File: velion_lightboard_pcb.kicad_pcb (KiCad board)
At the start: 2 copper layers, 100 x 100 mm, 137 parts, among them J1 Conn_01x04, J10 Conn_01x04, J11 Conn_01x04, J12 Conn_01x03, J13 Conn_01x03, J14 Conn_01x03, J15 Conn_01x03, J16 Conn_01x03, J17 Conn_01x04, J2 Conn_01x04, J3 Conn_01x03, J4 Conn_01x04, J5 Conn_01x04, J6 Conn_01x04, J7 Conn_01x03, J8 Conn_01x03, J9 Conn_01x03, Q1 BSS123-7-F, Q10 BSS123-7-F, Q11 BSS123-7-F, Q12 BSS123-7-F, Q13 NMOS, Q14 NMOS, Q15 NMOS, Q16 NMOS, Q17 NMOS, Q18 NMOS, Q19 NMOS, Q2 BSS123-7-F, Q20 NMOS, Q3 BSS123-7-F, Q4 BSS123-7-F, Q5 BSS123-7-F, Q6 BSS123-7-F, Q7 BSS123-7-F, Q8 BSS123-7-F, Q9 BSS123-7-F, U1 ESP32-C3_SUPERMINI_TH, U10 LM2104DR, U11 ADS1115IDGS, U12 MCP23017_SO, U13 ADS1115IDGS, U14 TJA1051T-3, U2 MCP6L01x-xOT, U3 MCP6L01x-xOT, U4 MCP6L01x-xOT, U5 LM2104DR, U6 LM2104DR, U7 LM2104DR, U8 LM2104DR, U9 LM2104DR

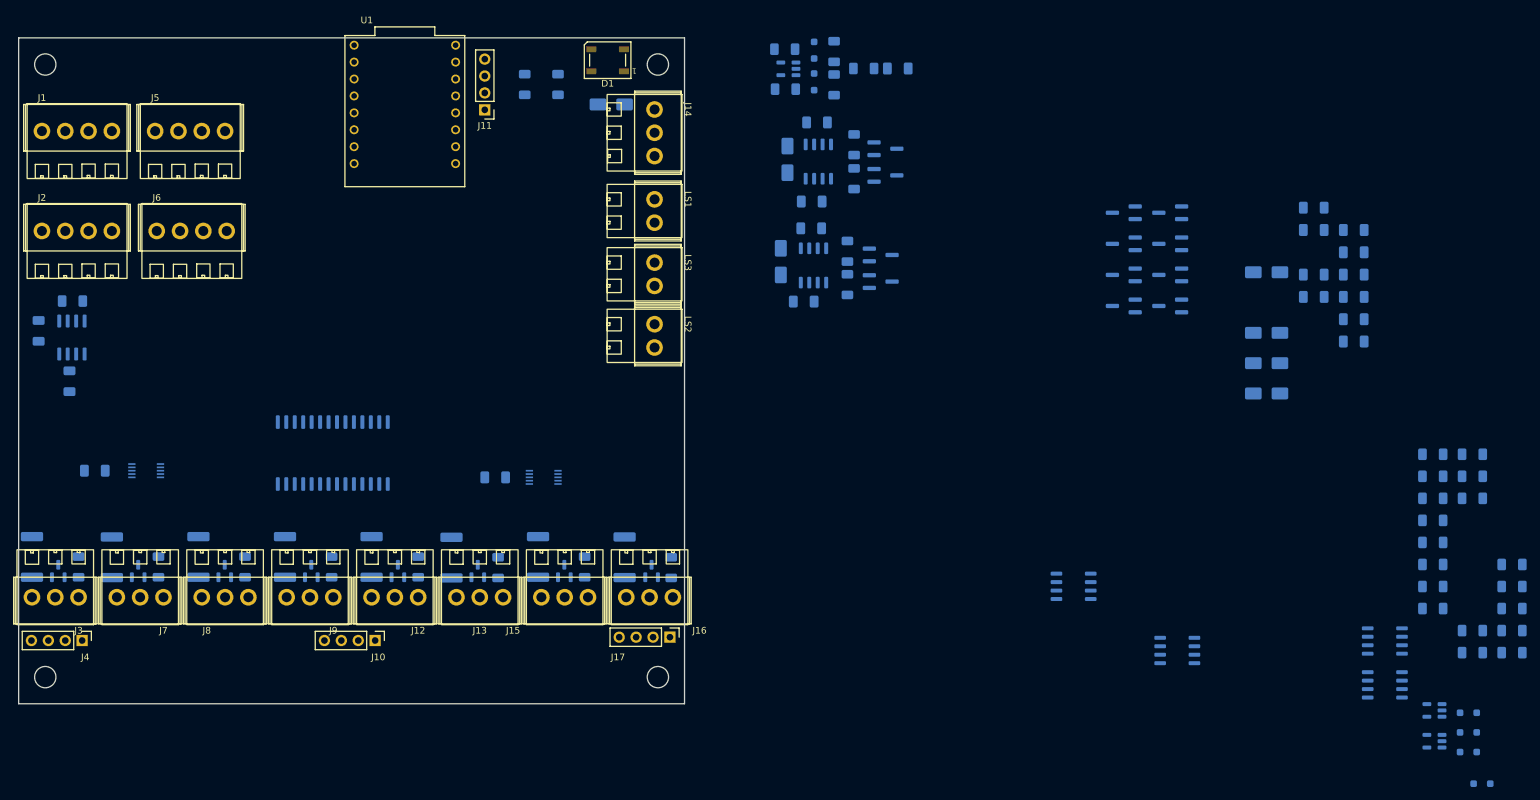
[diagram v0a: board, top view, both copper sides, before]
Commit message: routed the PCB, need review
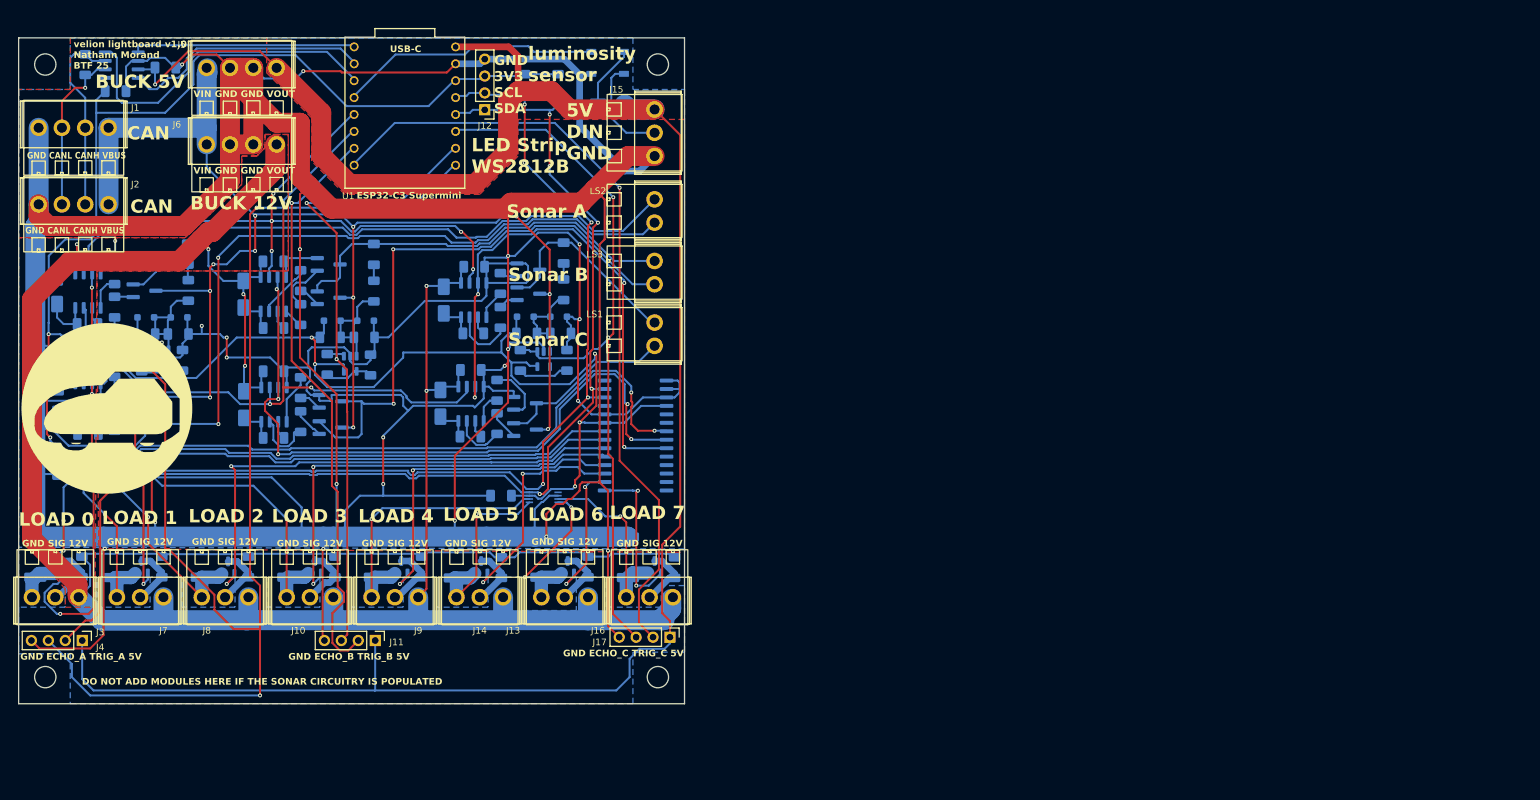
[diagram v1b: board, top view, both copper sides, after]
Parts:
- added G***: LOGO, velion_mainboard:silhouette, F.Cu at (63.2, 111.0)
- D1: moved to B.Cu
- moved R18 186.9 mm to (92.3, 86.5), turned to -90 degrees
- moved R21 186.5 mm to (92.3, 91.5), turned to 90 degrees
- moved R20 184.9 mm to (92.3, 102.5), turned to -90 degrees
- moved R19 184.6 mm to (92.3, 107.6), turned to 90 degrees
- moved D7 180.5 mm to (97.1, 92.5), turned to 0 degrees
- moved R24 177.9 mm to (96.8, 95.0)
- moved D6 176.8 mm to (102.1, 92.5)
- moved R17 172.7 mm to (103.3, 88.0), turned to 90 degrees
- moved U7 170.9 mm to (99.8, 98.9), turned to -90 degrees
- moved U11 170.6 mm to (88.3, 105.1), turned to -90 degrees
- moved R22 166.9 mm to (96.3, 99.0), turned to 90 degrees
- moved C11 164.1 mm to (88.3, 110.1), turned to 0 degrees
- moved C12 162.6 mm to (88.3, 93.6), turned to 0 degrees
- moved C13 162.6 mm to (88.3, 100.1), turned to 0 degrees
- moved C10 162.3 mm to (88.2, 83.6), turned to 0 degrees
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- renumbered C19 to C0, C7 to C1, C1 to C10, C9 to C11, C3 to C12, C8 to C13, C10 to C14, C4 to C15, C11 to C16, C14 to C17, C12 to C18, C16 to C2, C13 to C3, C17 to C4, C18 to C6, C6 to C7, C2 to C8, C15 to C9, D12 to D0, D3 to D10, D9 to D12, D8 to D13, D7 to D2, D6 to D3, D14 to D4, D13 to D5, D5 to D6, D4 to D7, D10 to D8, D2 to D9, J9 to J10, J10 to J11, J11 to J12, J15 to J13, J13 to J14, J14 to J15, J12 to J9, LS3 to LS1, LS1 to LS2, LS2 to LS3, Q13 to Q0, Q10 to Q1, Q7 to Q10, Q16 to Q11, Q17 to Q12, Q2 to Q13, Q1 to Q14, Q8 to Q15, Q5 to Q16, Q18 to Q17, Q19 to Q18, Q20 to Q19, Q9 to Q2, Q12 to Q3, Q11 to Q4, Q14 to Q5, Q15 to Q6, Q3 to Q7, Q4 to Q8, Q6 to Q9, R29 to R0, R30 to R1, R12 to R10, R22 to R11, R25 to R12, R36 to R13, R34 to R14, R35 to R15, R31 to R16, R26 to R17, R6 to R18, R9 to R19, R32 to R2, R10 to R20, R5 to R21, R14 to R22, R13 to R23, R27 to R24, R15 to R25, R38 to R26, R40 to R27, R39 to R28, R37 to R29, R33 to R3, R20 to R30, R19 to R31, R24 to R32, R18 to R33, R28 to R34, R43 to R35, R42 to R36, R41 to R37, R44 to R38, R2 to R39, R11 to R4, R4 to R40, R1 to R41, R7 to R42, R3 to R43, R45 to R44, R46 to R45, R23 to R5, R17 to R6, R8 to R7, R21 to R8, R16 to R9, U3 to U10, U8 to U11, U5 to U12, U6 to U13, U13 to U14, U12 to U2, U10 to U3, U9 to U4, U4 to U5, U11 to U6, U2 to U7, U14 to U8, U7 to U9
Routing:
- net GND: track 0.00 -> 1058.9 mm, vias 0 -> 27
- net +12V: track 0.00 -> 536.6 mm, vias 0 -> 7
- net +3.3V: track 0.00 -> 331.2 mm, vias 0 -> 9
- net +5V: track 0.00 -> 315.8 mm, vias 0 -> 1
- net VBUS: track 0.00 -> 212.6 mm, vias 0 -> 11
- net ECHO_A: track 0.00 -> 199.2 mm, vias 0 -> 3
- net PIEZO_PWM_HALF_Y: track 0.00 -> 158.8 mm, vias 0 -> 4
- net SDA: track 0.00 -> 154.0 mm, vias 0 -> 5
- net SCL: track 0.00 -> 150.2 mm, vias 0 -> 5
- net EN_PIEZO_A: track 0.00 -> 129.0 mm, vias 0 -> 5
- net TRIG_C: track 0.00 -> 118.7 mm, vias 0 -> 1
- net MOSFET_GATE_0: track 0.00 -> 114.3 mm, vias 0 -> 2
- net Net-(LS1-Pad2): track 0.00 -> 112.2 mm, vias 0 -> 2
- net ECHO_C: track 0.00 -> 111.5 mm, vias 0 -> 2
- net EN_PIEZO_B: track 0.00 -> 104.9 mm, vias 0 -> 5
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- added copper zone on B.Cu, net +12V
- added copper zone on F.Cu, net +12V
- added copper zone on B.Cu, net GND
- added copper zone on F.Cu, net GND
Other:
- board text added: "5V DIN GND"
- board text added: "BUCK 12V"
- board text added: "BUCK 5V"
- board text added: "CAN"
- board text added: "DO NOT ADD MODULES HERE IF THE SONAR CIRCUITRY IS POPULATED"
- board text added: "ESP32-C3 Supermini"
- board text added: "GND 3V3 SCL SDA"
- board text added: "GND CANL CANH VBUS"
- board text added: "GND ECHO_A TRIG_A 5V"
- board text added: "GND ECHO_B TRIG_B 5V"
- board text added: "GND ECHO_C TRIG_C 5V"
- board text added: "GND SIG 12V"
- board text added: "LED Strip WS2812B"
- board text added: "LOAD 0"
- board text added: "LOAD 1"
- board text added: "LOAD 2"
- board text added: "LOAD 3"
- board text added: "LOAD 4"
- board text added: "LOAD 5"
- board text added: "LOAD 6"
- board text added: "LOAD 7"
- board text added: "Sonar A"
- board text added: "Sonar B"
- board text added: "Sonar C"
- board text added: "USB-C"
- board text added: "VIN GND GND VOUT"
- board text added: "luminosity sensor"
- board text added: "velion lightboard v1.0 Nathann Morand BTF 25"

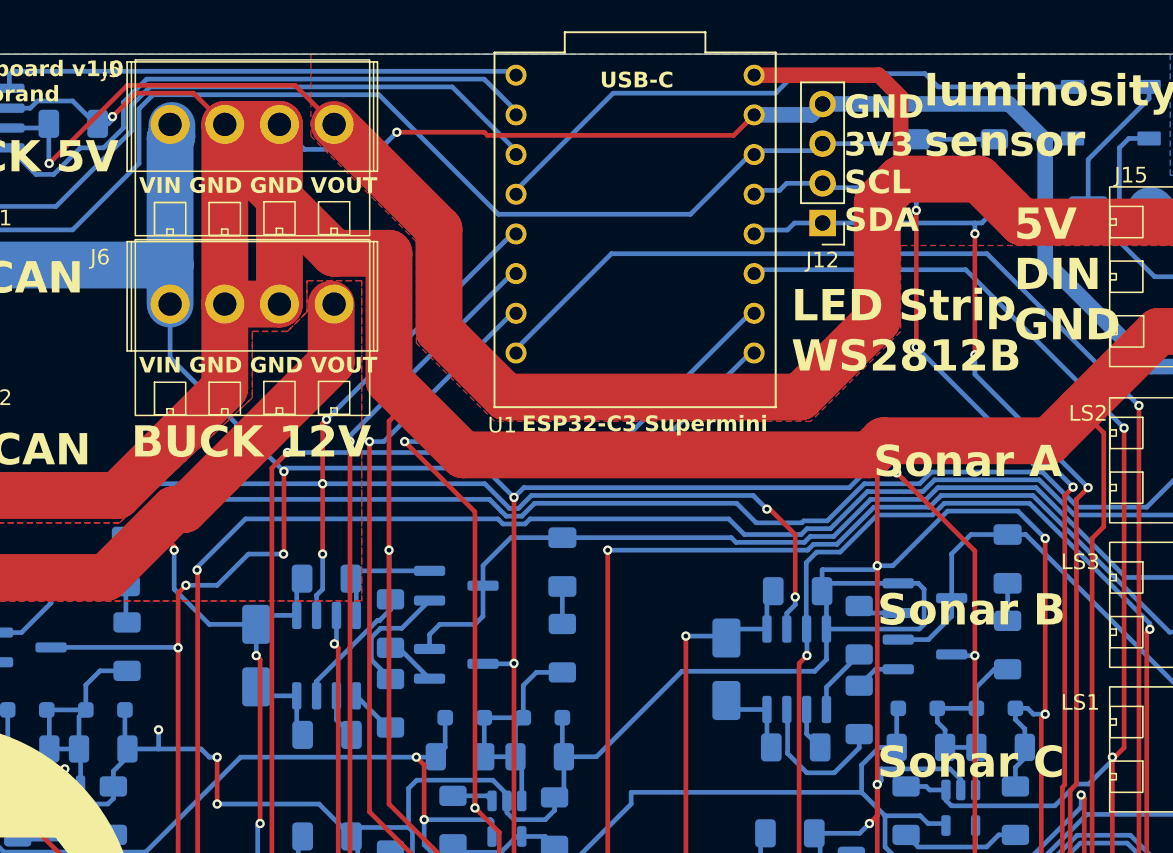
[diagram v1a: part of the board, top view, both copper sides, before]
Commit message: generated fab file, added capacitor for low pass/antialiasing in  Sonar
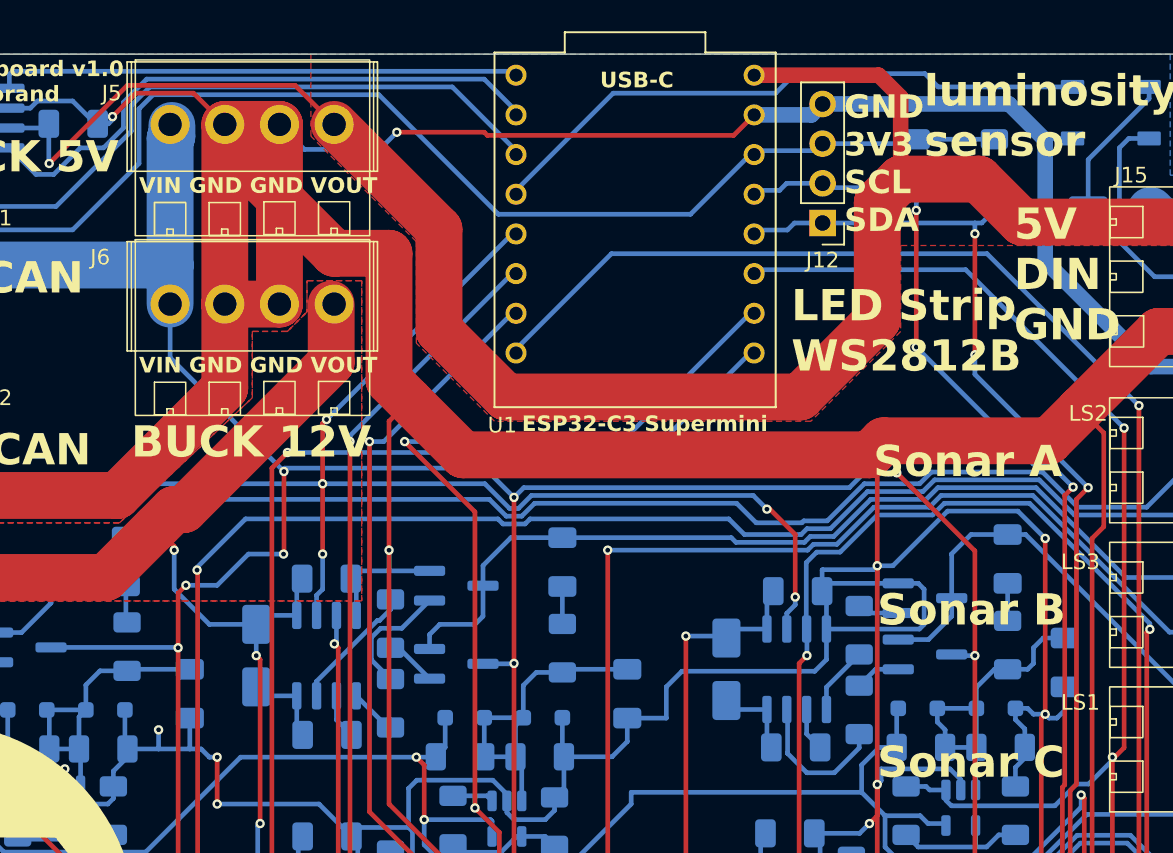
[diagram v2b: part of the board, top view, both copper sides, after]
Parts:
- added C19: 1nF, Capacitor_SMD:C_1206_3216Metric_Pad1.33x1.80mm_HandSolder, B.Cu at (79.5, 90.9)
- added C20: 1nF, Capacitor_SMD:C_1206_3216Metric_Pad1.33x1.80mm_HandSolder, B.Cu at (107.5, 90.9)
- added C21: 1nF, Capacitor_SMD:C_1206_3216Metric_Pad1.33x1.80mm_HandSolder, B.Cu at (135.5, 88.9)
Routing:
- net GND: track 1058.9 -> 1066.0 mm
- net Net-(D2-A): track 16.3 -> 21.3 mm
- net Net-(D6-A): track 17.6 -> 21.8 mm
- net Net-(D10-A): track 16.7 -> 20.7 mm

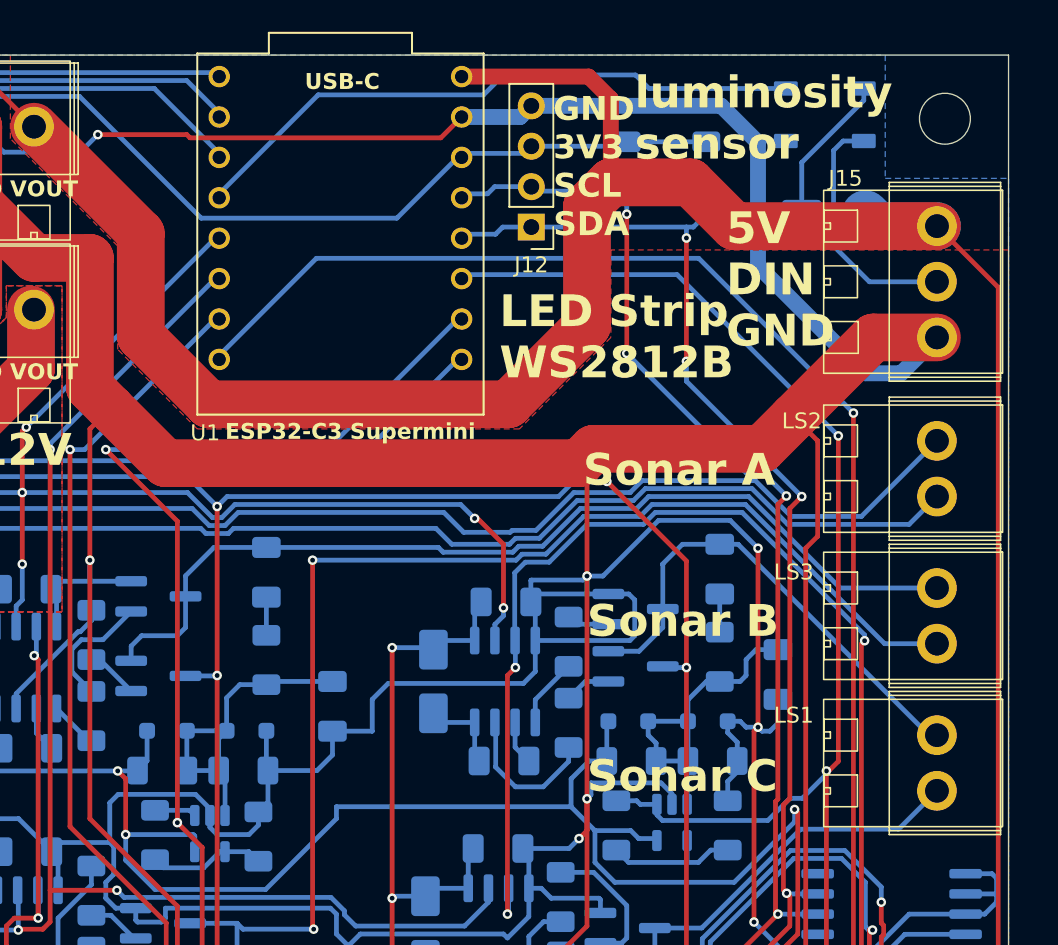
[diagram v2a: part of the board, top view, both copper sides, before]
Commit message: replaced the light sensor pin header by a standard bornier
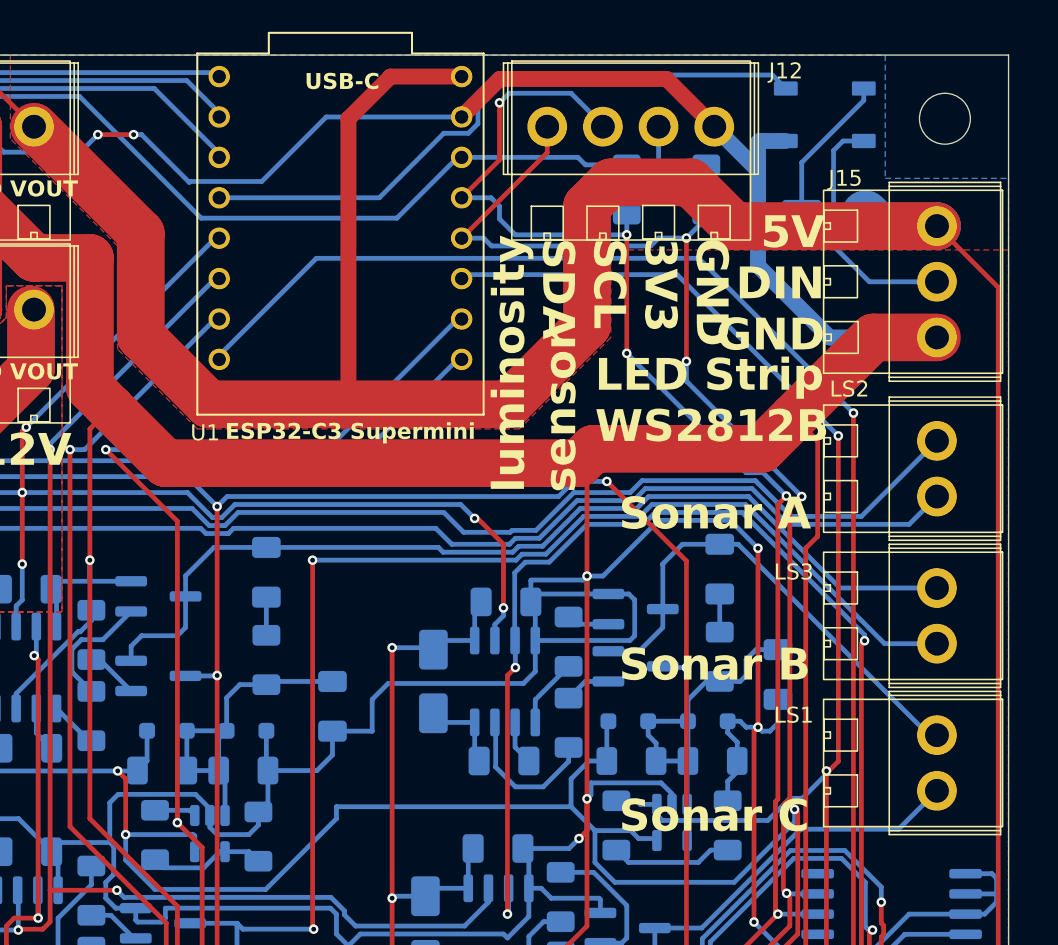
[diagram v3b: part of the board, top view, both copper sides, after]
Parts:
- J12: footprint Connector_PinHeader_2.54mm:PinHeader_1x04_P2.54mm_Vertical -> velion_mainboard:15EDG-4P
- moved J12 6.39 mm to (121.0, 54.5), turned to 0 degrees
- moved R2 1.45 mm to (126.0, 58.5)
- moved R3 1.45 mm to (131.0, 58.5)
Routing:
- net SCL: track 150.2 -> 164.7 mm, vias 5 -> 6
- net +5V: track 315.8 -> 326.8 mm
- net SDA: track 154.0 -> 162.0 mm
- net +3.3V: track 331.2 -> 334.2 mm
- net GND: track 1066.0 -> 1067.3 mm, vias 27 -> 28
- net RGBLED_DIN: track 39.3 -> 40.0 mm

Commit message: adding BOM for mouser
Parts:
- U14, U6: footprint Package_SO:TSSOP-10_3x3mm_P0.5mm -> Package_SO:VSSOP-10_3x3mm_P0.5mm
